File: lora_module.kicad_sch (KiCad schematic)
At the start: 1 part, among them U1 Ai-Thinker-Ra-02

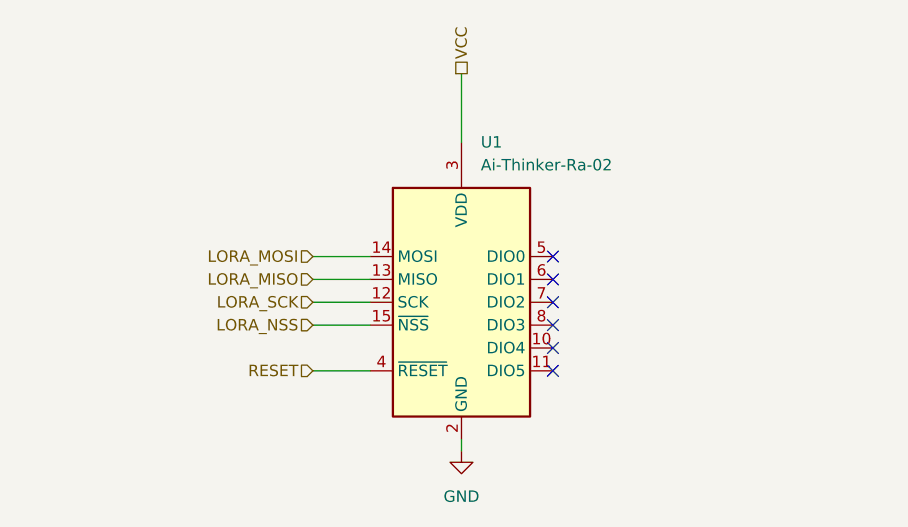
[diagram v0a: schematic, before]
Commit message: feat(lora): add decoupling caps C9/C10 and tie power rails
Adds two Device:C_Small decoupling capacitors (C9, C10) on the LoRa module supply, and ties the module to power:+3.3V and power:GND explicitly. Removes the VCC hierarchical label now that the rail is referenced directly via the power symbol, and repositions the LORA_SCK hierarchical label to match the new layout.
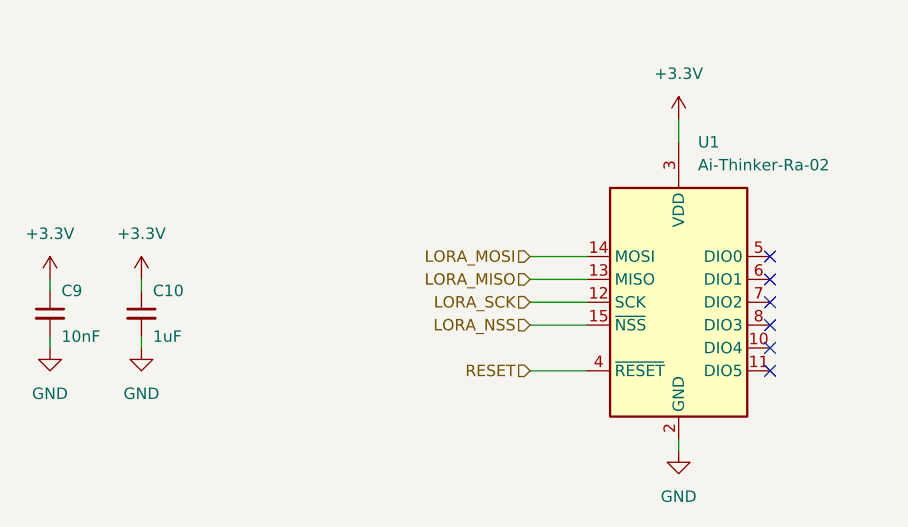
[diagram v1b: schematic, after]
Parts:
- added C10: 1uF, Capacitor_SMD:C_0603_1608Metric_Pad1.08x0.95mm_HandSolder, symbol Device:C_Small
- added C9: 10nF, Capacitor_SMD:C_0603_1608Metric_Pad1.08x0.95mm_HandSolder, symbol Device:C_Small
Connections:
- net GND: now also C10.2, C9.2
- net VCC renamed +3.3V
- net +3.3V: now also C10.1, C9.1
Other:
- moved on the sheet: U1

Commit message: fix(fixed_annotation): sorted by x position
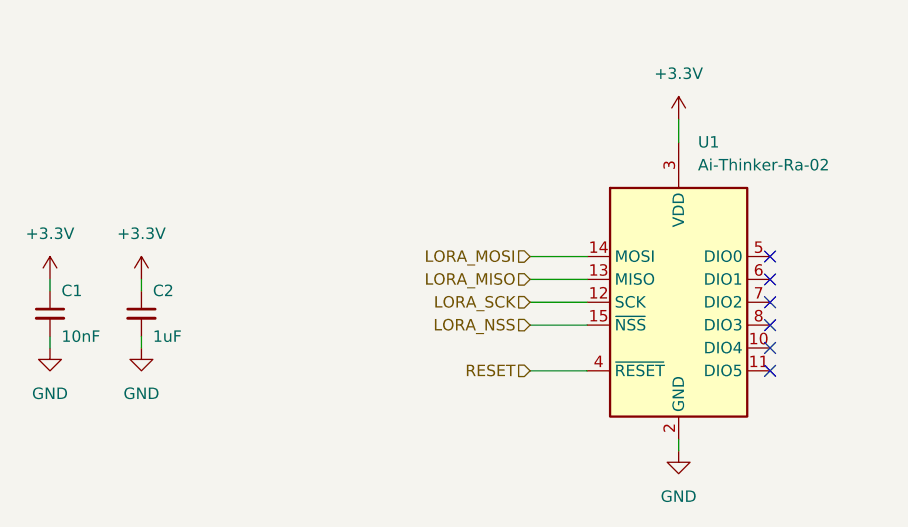
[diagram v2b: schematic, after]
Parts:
- renumbered C9 to C1, C10 to C2
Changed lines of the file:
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@@
 		(dnp no)
 		(fields_autoplaced yes)
-		(property "Reference" "#PWR08"
+		(property "Reference" "#PWR05"
 			(at 170.18 86.36 0)
 			(hide yes)
@@
 			(project "HW"
 				(path "/01550cd7-b424-469c-925b-c370f3609cd4/2dab47df-4ca4-4373-b48e-0efc8c61f605"
-					(reference "#PWR08")
+					(reference "#PWR05")
 					(unit 1)
 				)
@@
 		(dnp no)
 		(fields_autoplaced yes)
-		(property "Reference" "#PWR045"
+		(property "Reference" "#PWR03"
 			(at 110.49 104.14 0)
 			(hide yes)
@@
 			(project "HW"
 				(path "/01550cd7-b424-469c-925b-c370f3609cd4/2dab47df-4ca4-4373-b48e-0efc8c61f605"
-					(reference "#PWR045")
+					(reference "#PWR03")
 					(unit 1)
 				)
@@
 		(in_pos_files yes)
 		(dnp no)
-		(property "Reference" "C9"
+		(property "Reference" "C1"
 			(at 101.6 101.6 0)
 			(show_name no)
@@
 			(project "HW"
 				(path "/01550cd7-b424-469c-925b-c370f3609cd4/2dab47df-4ca4-4373-b48e-0efc8c61f605"
-					(reference "C9")
+					(reference "C1")
 					(unit 1)
 				)
@@
 		(dnp no)
 		(fields_autoplaced yes)
-		(property "Reference" "#PWR024"
+		(property "Reference" "#PWR06"
 			(at 170.18 125.73 0)
 			(hide yes)
@@
 			(project "HW"
 				(path "/01550cd7-b424-469c-925b-c370f3609cd4/2dab47df-4ca4-4373-b48e-0efc8c61f605"
-					(reference "#PWR024")
+					(reference "#PWR06")
 					(unit 1)
 				)
@@
 		(dnp no)
 		(fields_autoplaced yes)
-		(property "Reference" "#PWR042"
+		(property "Reference" "#PWR02"
 			(at 100.33 114.3 0)
 			(hide yes)
@@
 			(project "HW"
 				(path "/01550cd7-b424-469c-925b-c370f3609cd4/2dab47df-4ca4-4373-b48e-0efc8c61f605"
-					(reference "#PWR042")
+					(reference "#PWR02")
 					(unit 1)
 				)
@@
 		(in_pos_files yes)
 		(dnp no)
-		(property "Reference" "C10"
+		(property "Reference" "C2"
 			(at 111.76 101.6 0)
 			(show_name no)
@@
 			(project "HW"
 				(path "/01550cd7-b424-469c-925b-c370f3609cd4/2dab47df-4ca4-4373-b48e-0efc8c61f605"
-					(reference "C10")
+					(reference "C2")
 					(unit 1)
 				)
@@
 		(dnp no)
 		(fields_autoplaced yes)
-		(property "Reference" "#PWR044"
+		(property "Reference" "#PWR01"
 			(at 100.33 104.14 0)
 			(hide yes)
@@
 			(project "HW"
 				(path "/01550cd7-b424-469c-925b-c370f3609cd4/2dab47df-4ca4-4373-b48e-0efc8c61f605"
-					(reference "#PWR044")
+					(reference "#PWR01")
 					(unit 1)
 				)
@@
 		(dnp no)
 		(fields_autoplaced yes)
-		(property "Reference" "#PWR043"
+		(property "Reference" "#PWR04"
 			(at 110.49 114.3 0)
 			(hide yes)
@@
 			(project "HW"
 				(path "/01550cd7-b424-469c-925b-c370f3609cd4/2dab47df-4ca4-4373-b48e-0efc8c61f605"
-					(reference "#PWR043")
-					(unit 1)
-				)
+					(reference "#PWR04")
+					(unit 1)
+				)
